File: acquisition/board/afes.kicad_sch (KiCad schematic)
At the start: 0 parts

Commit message: Continued initial design
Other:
- company: (none) -> A. Zonenberg
- title: (none) -> Digitizer board
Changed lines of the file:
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@@
 (kicad_sch (version 20211123) (generator eeschema)
   (paper "A4")
+  (title_block
+    (title "Digitizer board")
+    (date "2022-06-22")
+    (rev "0.1")
+    (company "A. Zonenberg")
+  )
   (hierarchical_label "IN6_P" (shape output) (at 88.9 93.98 0)
     (effects (font (size 1.27 1.27)) (justify left))

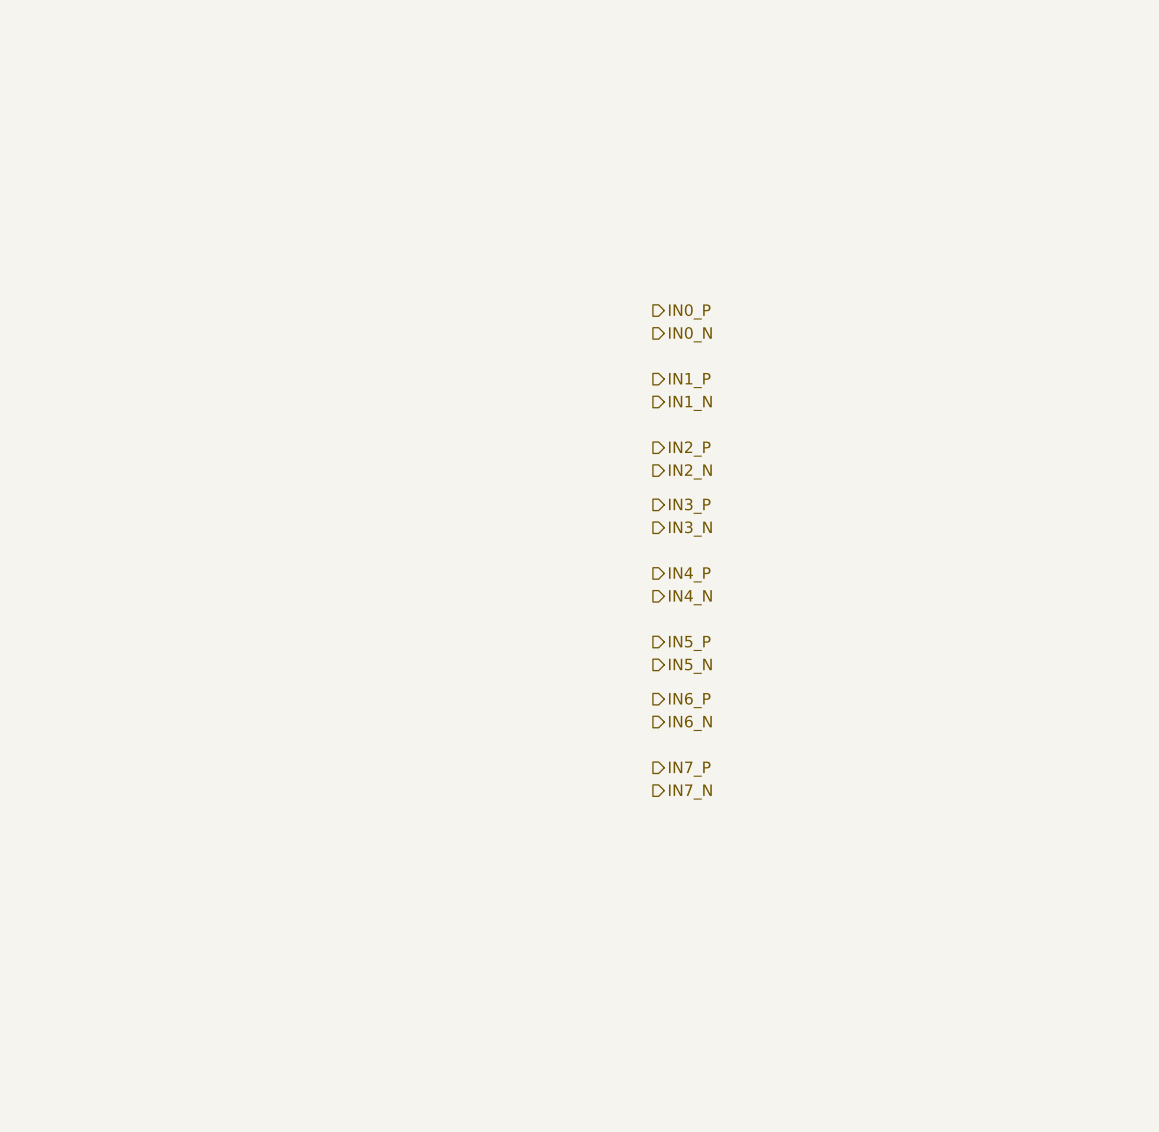
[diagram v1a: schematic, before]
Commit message: Updated schematic with a lot of level shifting and support stuff, power decoupling, etc. Almost done except power supply and protection diodes
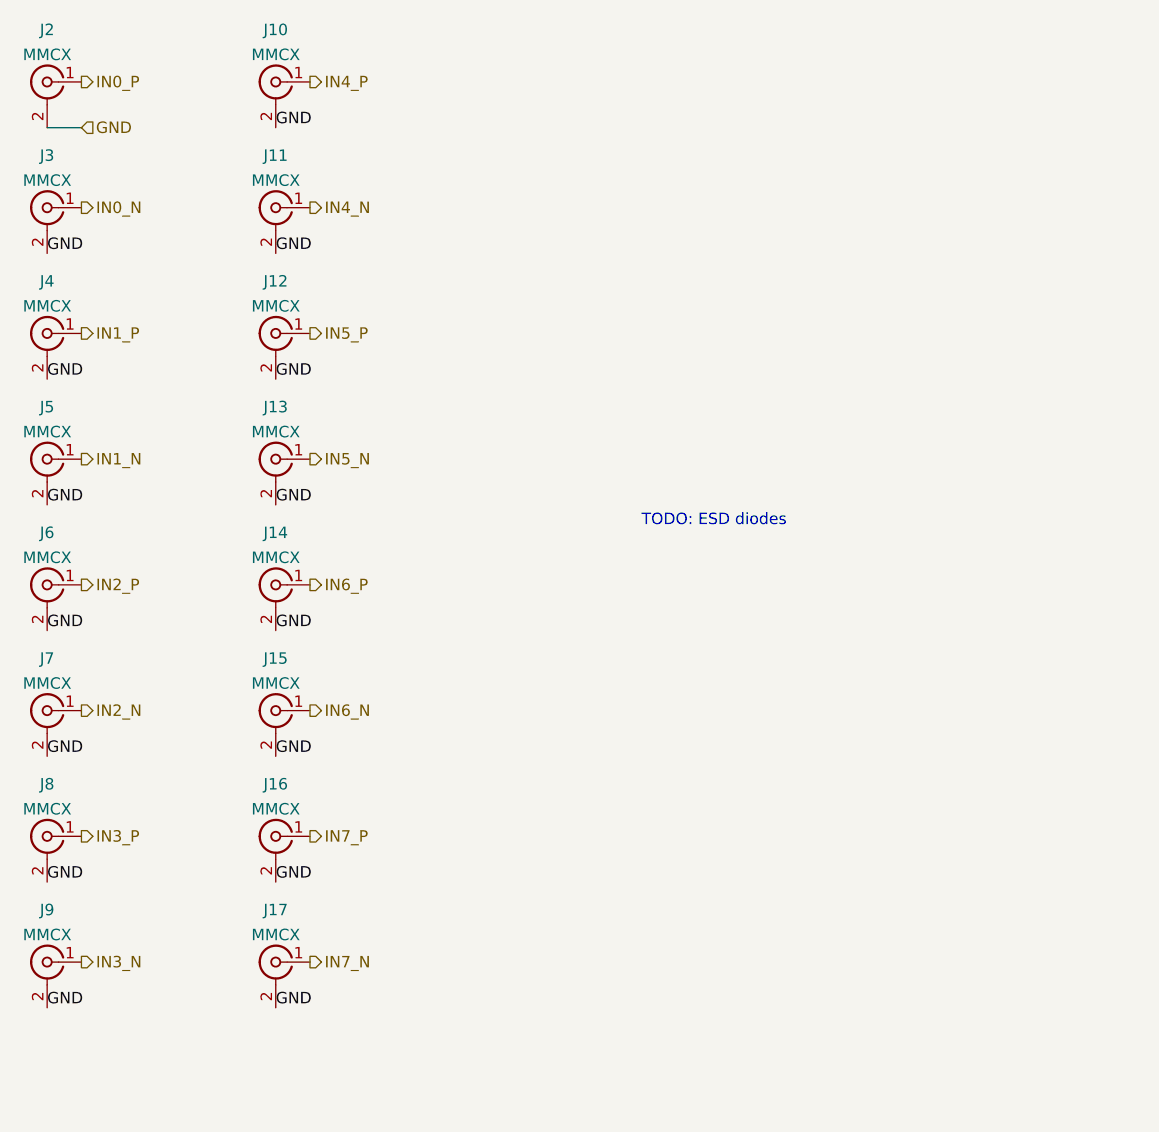
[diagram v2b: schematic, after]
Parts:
- added J10, J11, J12, J13, J14, J15, J16, J17, J2, J3, J4, J5, J6, J7, J8, J9: MMCX, symbol conn:CONN_COAXIAL
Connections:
- net IN0_N: now also J3.1 (In)
- net IN0_P: now also J2.1 (In)
- net IN1_N: now also J5.1 (In)
- net IN1_P: now also J4.1 (In)
- net IN2_N: now also J7.1 (In)
- net IN2_P: now also J6.1 (In)
- net IN3_N: now also J9.1 (In)
- net IN3_P: now also J8.1 (In)
- net IN4_N: now also J11.1 (In)
- net IN4_P: now also J10.1 (In)
- net IN5_N: now also J13.1 (In)
- net IN5_P: now also J12.1 (In)
- net IN6_N: now also J15.1 (In)
- net IN6_P: now also J14.1 (In)
- net IN7_N: now also J17.1 (In)
- net IN7_P: now also J16.1 (In)
- new net GND: J10.2 (Ext), J11.2 (Ext), J12.2 (Ext), J13.2 (Ext), J14.2 (Ext), J15.2 (Ext), J16.2 (Ext), J17.2 (Ext), J2.2 (Ext), J3.2 (Ext), J4.2 (Ext), J5.2 (Ext), J6.2 (Ext), J7.2 (Ext), J8.2 (Ext), J9.2 (Ext)
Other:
- note added: "TODO: ESD diodes"

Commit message: Lots of progress on power supply design, added a bunch of test points, etc
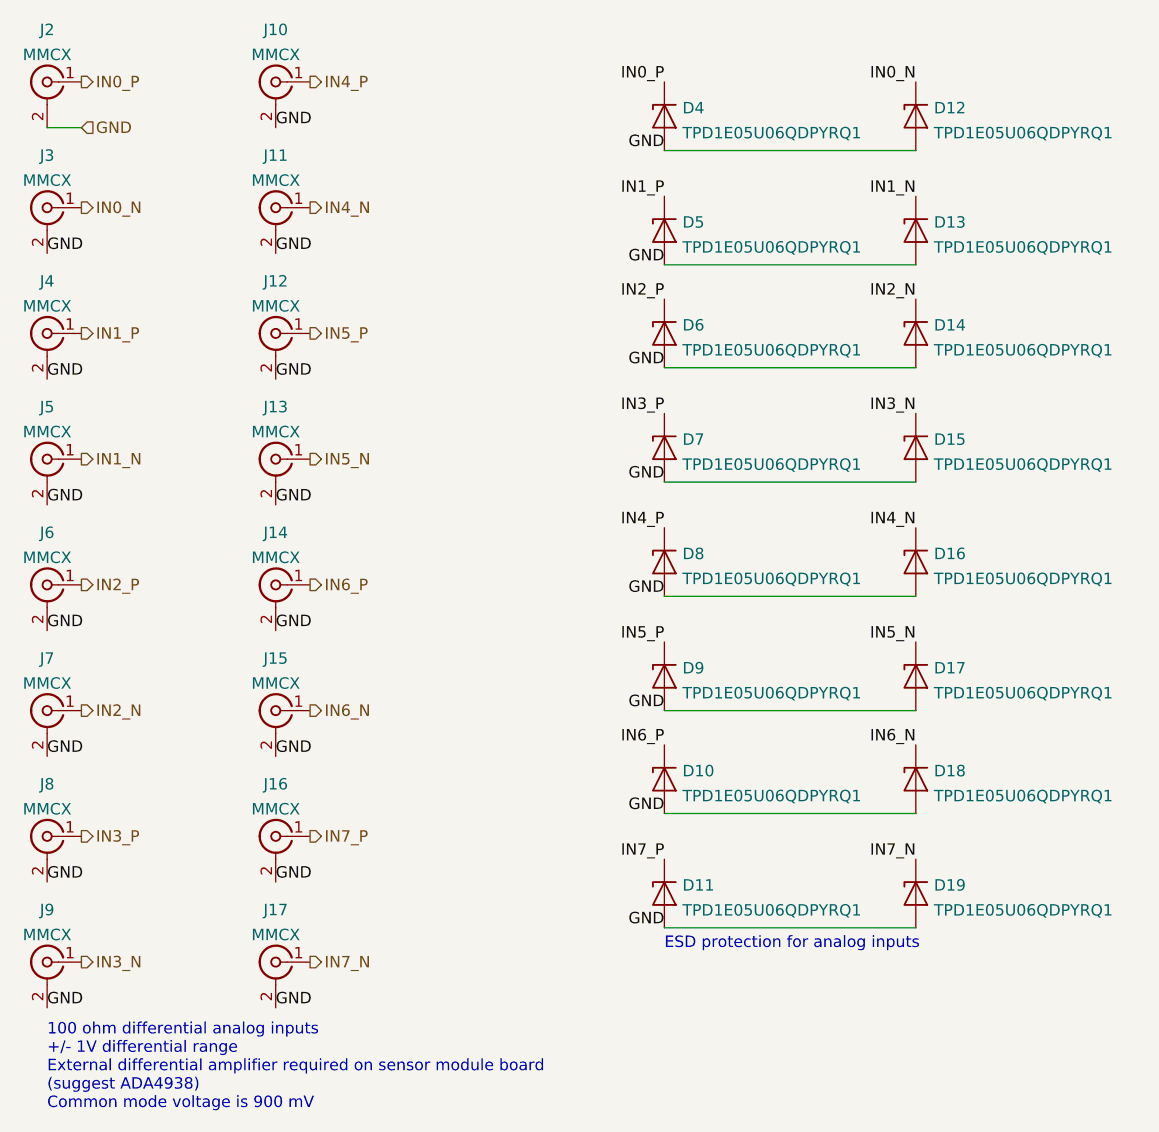
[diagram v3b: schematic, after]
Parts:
- added D10, D11, D12, D13, D14, D15, D16, D17, D18, D19, D4, D5, D6, D7, D8, D9: TPD1E05U06QDPYRQ1, symbol device:D_Zener
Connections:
- net GND: now also D10.2 (A), D11.2 (A), D12.2 (A), D13.2 (A), D14.2 (A), D15.2 (A), D16.2 (A), D17.2 (A), D18.2 (A), D19.2 (A), D4.2 (A), D5.2 (A), D6.2 (A), D7.2 (A), D8.2 (A), D9.2 (A)
- net IN0_N: now also D12.1 (K)
- net IN0_P: now also D4.1 (K)
- net IN1_N: now also D13.1 (K)
- net IN1_P: now also D5.1 (K)
- net IN2_N: now also D14.1 (K)
- net IN2_P: now also D6.1 (K)
- net IN3_N: now also D15.1 (K)
- net IN3_P: now also D7.1 (K)
- net IN4_N: now also D16.1 (K)
- net IN4_P: now also D8.1 (K)
- net IN5_N: now also D17.1 (K)
- net IN5_P: now also D9.1 (K)
- net IN6_N: now also D18.1 (K)
- net IN6_P: now also D10.1 (K)
- net IN7_N: now also D19.1 (K)
- net IN7_P: now also D11.1 (K)
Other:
- note added: "100 ohm differential analog inputs +/- 1V differential range External differential amplifier required on sensor module board (suggest ADA4938) Common mode voltage is 900 mV"
- note added: "ESD protection for analog inputs"
- note removed: "TODO: ESD diodes"

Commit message: More power supply work, added PLL loop filter, soft start, began assigning footprints
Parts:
- J10, J11, J12, J13, J14, J15, J16, J17, J2, J3, J4, J5, J6, J7, J8, J9: footprint (none) -> azonenberg_pcb:CONN_MMCX_J_P_H_ST_EM1
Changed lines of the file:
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@@
   (title_block
     (title "Digitizer board")
-    (date "2022-07-05")
+    (date "2022-07-08")
     (rev "0.1")
     (company "A. Zonenberg")
@@
     (property "Reference" "J17" (id 0) (at 46.9899 117.3969 0))
     (property "Value" "MMCX" (id 1) (at 46.9899 120.172 0))
-    (property "Footprint" "" (id 2) (at 46.99 123.19 0)
+    (property "Footprint" "azonenberg_pcb:CONN_MMCX_J_P_H_ST_EM1" (id 2) (at 46.99 123.19 0)
       (effects (font (size 1.27 1.27)) hide)
     )
@@
     (property "Reference" "J4" (id 0) (at 21.5899 47.5469 0))
     (property "Value" "MMCX" (id 1) (at 21.5899 50.322 0))
-    (property "Footprint" "" (id 2) (at 21.59 53.34 0)
+    (property "Footprint" "azonenberg_pcb:CONN_MMCX_J_P_H_ST_EM1" (id 2) (at 21.59 53.34 0)
       (effects (font (size 1.27 1.27)) hide)
     )
@@
     (property "Reference" "J10" (id 0) (at 46.9899 19.6069 0))
     (property "Value" "MMCX" (id 1) (at 46.9899 22.382 0))
-    (property "Footprint" "" (id 2) (at 46.99 25.4 0)
+    (property "Footprint" "azonenberg_pcb:CONN_MMCX_J_P_H_ST_EM1" (id 2) (at 46.99 25.4 0)
       (effects (font (size 1.27 1.27)) hide)
     )
@@
     (property "Reference" "J16" (id 0) (at 46.9899 103.4269 0))
     (property "Value" "MMCX" (id 1) (at 46.9899 106.202 0))
-    (property "Footprint" "" (id 2) (at 46.99 109.22 0)
+    (property "Footprint" "azonenberg_pcb:CONN_MMCX_J_P_H_ST_EM1" (id 2) (at 46.99 109.22 0)
       (effects (font (size 1.27 1.27)) hide)
     )
@@
     (property "Reference" "J3" (id 0) (at 21.5899 33.5769 0))
     (property "Value" "MMCX" (id 1) (at 21.5899 36.352 0))
-    (property "Footprint" "" (id 2) (at 21.59 39.37 0)
+    (property "Footprint" "azonenberg_pcb:CONN_MMCX_J_P_H_ST_EM1" (id 2) (at 21.59 39.37 0)
       (effects (font (size 1.27 1.27)) hide)
     )
@@
     (property "Reference" "J8" (id 0) (at 21.5899 103.4269 0))
     (property "Value" "MMCX" (id 1) (at 21.5899 106.202 0))
-    (property "Footprint" "" (id 2) (at 21.59 109.22 0)
+    (property "Footprint" "azonenberg_pcb:CONN_MMCX_J_P_H_ST_EM1" (id 2) (at 21.59 109.22 0)
       (effects (font (size 1.27 1.27)) hide)
     )
@@
     (property "Reference" "J11" (id 0) (at 46.9899 33.5769 0))
     (property "Value" "MMCX" (id 1) (at 46.9899 36.352 0))
-    (property "Footprint" "" (id 2) (at 46.99 39.37 0)
+    (property "Footprint" "azonenberg_pcb:CONN_MMCX_J_P_H_ST_EM1" (id 2) (at 46.99 39.37 0)
       (effects (font (size 1.27 1.27)) hide)
     )
@@
     (property "Reference" "J5" (id 0) (at 21.5899 61.5169 0))
     (property "Value" "MMCX" (id 1) (at 21.5899 64.292 0))
-    (property "Footprint" "" (id 2) (at 21.59 67.31 0)
+    (property "Footprint" "azonenberg_pcb:CONN_MMCX_J_P_H_ST_EM1" (id 2) (at 21.59 67.31 0)
       (effects (font (size 1.27 1.27)) hide)
     )
@@
     (property "Reference" "J2" (id 0) (at 21.5899 19.6069 0))
     (property "Value" "MMCX" (id 1) (at 21.5899 22.382 0))
-    (property "Footprint" "" (id 2) (at 21.59 25.4 0)
+    (property "Footprint" "azonenberg_pcb:CONN_MMCX_J_P_H_ST_EM1" (id 2) (at 21.59 25.4 0)
       (effects (font (size 1.27 1.27)) hide)
     )
@@
     (property "Reference" "J7" (id 0) (at 21.5899 89.4569 0))
     (property "Value" "MMCX" (id 1) (at 21.5899 92.232 0))
-    (property "Footprint" "" (id 2) (at 21.59 95.25 0)
+    (property "Footprint" "azonenberg_pcb:CONN_MMCX_J_P_H_ST_EM1" (id 2) (at 21.59 95.25 0)
       (effects (font (size 1.27 1.27)) hide)
     )
@@
     (property "Reference" "J14" (id 0) (at 46.9899 75.4869 0))
     (property "Value" "MMCX" (id 1) (at 46.9899 78.262 0))
-    (property "Footprint" "" (id 2) (at 46.99 81.28 0)
+    (property "Footprint" "azonenberg_pcb:CONN_MMCX_J_P_H_ST_EM1" (id 2) (at 46.99 81.28 0)
       (effects (font (size 1.27 1.27)) hide)
     )
@@
     (property "Reference" "J15" (id 0) (at 46.9899 89.4569 0))
     (property "Value" "MMCX" (id 1) (at 46.9899 92.232 0))
-    (property "Footprint" "" (id 2) (at 46.99 95.25 0)
+    (property "Footprint" "azonenberg_pcb:CONN_MMCX_J_P_H_ST_EM1" (id 2) (at 46.99 95.25 0)
       (effects (font (size 1.27 1.27)) hide)
     )
@@
     (property "Reference" "J13" (id 0) (at 46.9899 61.5169 0))
     (property "Value" "MMCX" (id 1) (at 46.9899 64.292 0))
-    (property "Footprint" "" (id 2) (at 46.99 67.31 0)
+    (property "Footprint" "azonenberg_pcb:CONN_MMCX_J_P_H_ST_EM1" (id 2) (at 46.99 67.31 0)
       (effects (font (size 1.27 1.27)) hide)
     )
@@
     (property "Reference" "J6" (id 0) (at 21.5899 75.4869 0))
     (property "Value" "MMCX" (id 1) (at 21.5899 78.262 0))
-    (property "Footprint" "" (id 2) (at 21.59 81.28 0)
+    (property "Footprint" "azonenberg_pcb:CONN_MMCX_J_P_H_ST_EM1" (id 2) (at 21.59 81.28 0)
       (effects (font (size 1.27 1.27)) hide)
     )
@@
     (property "Reference" "J12" (id 0) (at 46.9899 47.5469 0))
     (property "Value" "MMCX" (id 1) (at 46.9899 50.322 0))
-    (property "Footprint" "" (id 2) (at 46.99 53.34 0)
+    (property "Footprint" "azonenberg_pcb:CONN_MMCX_J_P_H_ST_EM1" (id 2) (at 46.99 53.34 0)
       (effects (font (size 1.27 1.27)) hide)
     )
@@
     (property "Reference" "J9" (id 0) (at 21.5899 117.3969 0))
     (property "Value" "MMCX" (id 1) (at 21.5899 120.172 0))
-    (property "Footprint" "" (id 2) (at 21.59 123.19 0)
-      (effects (font (size 1.27 1.27)) hide)
-    )
+    (property "Footprint" "azonenberg_pcb:CONN_MMCX_J_P_H_ST_EM1" (id 2) (at 21.59 123.19 0)
+      (effects (font (size 1.27 1.27)) hide)
+    )

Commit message: Finished footprint assignment
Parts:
- D10, D11, D12, D13, D14, D15, D16, D17, D18, D19, D4, D5, D6, D7, D8, D9: footprint (none) -> azonenberg_pcb:DFN_2_1x0.6_TI_DPY
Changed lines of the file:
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@@
   (title_block
     (title "Digitizer board")
-    (date "2022-07-17")
+    (date "2023-01-29")
     (rev "0.1")
     (company "A. Zonenberg")
@@
       (effects (font (size 1.27 1.27)) (justify right))
     )
-    (property "Footprint" "" (id 2) (at 118.11 66.04 0)
+    (property "Footprint" "azonenberg_pcb:DFN_2_1x0.6_TI_DPY" (id 2) (at 118.11 66.04 0)
       (effects (font (size 1.27 1.27)) hide)
     )
@@
       (effects (font (size 1.27 1.27)) (justify right))
     )
-    (property "Footprint" "" (id 2) (at 118.11 102.87 0)
+    (property "Footprint" "azonenberg_pcb:DFN_2_1x0.6_TI_DPY" (id 2) (at 118.11 102.87 0)
       (effects (font (size 1.27 1.27)) hide)
     )
@@
       (effects (font (size 1.27 1.27)) (justify right))
     )
-    (property "Footprint" "" (id 2) (at 118.11 53.34 0)
+    (property "Footprint" "azonenberg_pcb:DFN_2_1x0.6_TI_DPY" (id 2) (at 118.11 53.34 0)
       (effects (font (size 1.27 1.27)) hide)
     )
@@
       (effects (font (size 1.27 1.27)) (justify right))
     )
-    (property "Footprint" "" (id 2) (at 118.11 91.44 0)
+    (property "Footprint" "azonenberg_pcb:DFN_2_1x0.6_TI_DPY" (id 2) (at 118.11 91.44 0)
       (effects (font (size 1.27 1.27)) hide)
     )
@@
       (effects (font (size 1.27 1.27)) (justify right))
     )
-    (property "Footprint" "" (id 2) (at 118.11 29.21 0)
+    (property "Footprint" "azonenberg_pcb:DFN_2_1x0.6_TI_DPY" (id 2) (at 118.11 29.21 0)
       (effects (font (size 1.27 1.27)) hide)
     )
@@
       (effects (font (size 1.27 1.27)) (justify right))
     )
-    (property "Footprint" "" (id 2) (at 90.17 53.34 0)
+    (property "Footprint" "azonenberg_pcb:DFN_2_1x0.6_TI_DPY" (id 2) (at 90.17 53.34 0)
       (effects (font (size 1.27 1.27)) hide)
     )
@@
       (effects (font (size 1.27 1.27)) (justify right))
     )
-    (property "Footprint" "" (id 2) (at 118.11 115.57 0)
+    (property "Footprint" "azonenberg_pcb:DFN_2_1x0.6_TI_DPY" (id 2) (at 118.11 115.57 0)
       (effects (font (size 1.27 1.27)) hide)
     )
@@
       (effects (font (size 1.27 1.27)) (justify right))
     )
-    (property "Footprint" "" (id 2) (at 118.11 41.91 0)
+    (property "Footprint" "azonenberg_pcb:DFN_2_1x0.6_TI_DPY" (id 2) (at 118.11 41.91 0)
       (effects (font (size 1.27 1.27)) hide)
     )
@@
       (effects (font (size 1.27 1.27)) (justify right))
     )
-    (property "Footprint" "" (id 2) (at 118.11 78.74 0)
+    (property "Footprint" "azonenberg_pcb:DFN_2_1x0.6_TI_DPY" (id 2) (at 118.11 78.74 0)
       (effects (font (size 1.27 1.27)) hide)
     )
@@
       (effects (font (size 1.27 1.27)) (justify right))
     )
-    (property "Footprint" "" (id 2) (at 90.17 115.57 0)
+    (property "Footprint" "azonenberg_pcb:DFN_2_1x0.6_TI_DPY" (id 2) (at 90.17 115.57 0)
       (effects (font (size 1.27 1.27)) hide)
     )
@@
       (effects (font (size 1.27 1.27)) (justify right))
     )
-    (property "Footprint" "" (id 2) (at 90.17 29.21 0)
+    (property "Footprint" "azonenberg_pcb:DFN_2_1x0.6_TI_DPY" (id 2) (at 90.17 29.21 0)
       (effects (font (size 1.27 1.27)) hide)
     )
@@
       (effects (font (size 1.27 1.27)) (justify right))
     )
-    (property "Footprint" "" (id 2) (at 90.17 102.87 0)
+    (property "Footprint" "azonenberg_pcb:DFN_2_1x0.6_TI_DPY" (id 2) (at 90.17 102.87 0)
       (effects (font (size 1.27 1.27)) hide)
     )
@@
       (effects (font (size 1.27 1.27)) (justify right))
     )
-    (property "Footprint" "" (id 2) (at 90.17 66.04 0)
+    (property "Footprint" "azonenberg_pcb:DFN_2_1x0.6_TI_DPY" (id 2) (at 90.17 66.04 0)
       (effects (font (size 1.27 1.27)) hide)
     )
@@
       (effects (font (size 1.27 1.27)) (justify right))
     )
-    (property "Footprint" "" (id 2) (at 90.17 41.91 0)
+    (property "Footprint" "azonenberg_pcb:DFN_2_1x0.6_TI_DPY" (id 2) (at 90.17 41.91 0)
       (effects (font (size 1.27 1.27)) hide)
     )
@@
       (effects (font (size 1.27 1.27)) (justify right))
     )
-    (property "Footprint" "" (id 2) (at 90.17 78.74 0)
+    (property "Footprint" "azonenberg_pcb:DFN_2_1x0.6_TI_DPY" (id 2) (at 90.17 78.74 0)
       (effects (font (size 1.27 1.27)) hide)
     )
@@
       (effects (font (size 1.27 1.27)) (justify right))
     )
-    (property "Footprint" "" (id 2) (at 90.17 91.44 0)
-      (effects (font (size 1.27 1.27)) hide)
-    )
+    (property "Footprint" "azonenberg_pcb:DFN_2_1x0.6_TI_DPY" (id 2) (at 90.17 91.44 0)
+      (effects (font (size 1.27 1.27)) hide)
+    )
